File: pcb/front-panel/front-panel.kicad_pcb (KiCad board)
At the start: 2 copper layers, 85.7 x 19 mm, 31 parts, among them J1 HEADER-1x06, J2 HEADER-1x01, J3 HEADER-1x01, J4 HEADER-1x01, J5 HEADER-1x01, U1 ER-OLED1602-4W, U2 LT1109CS8-12

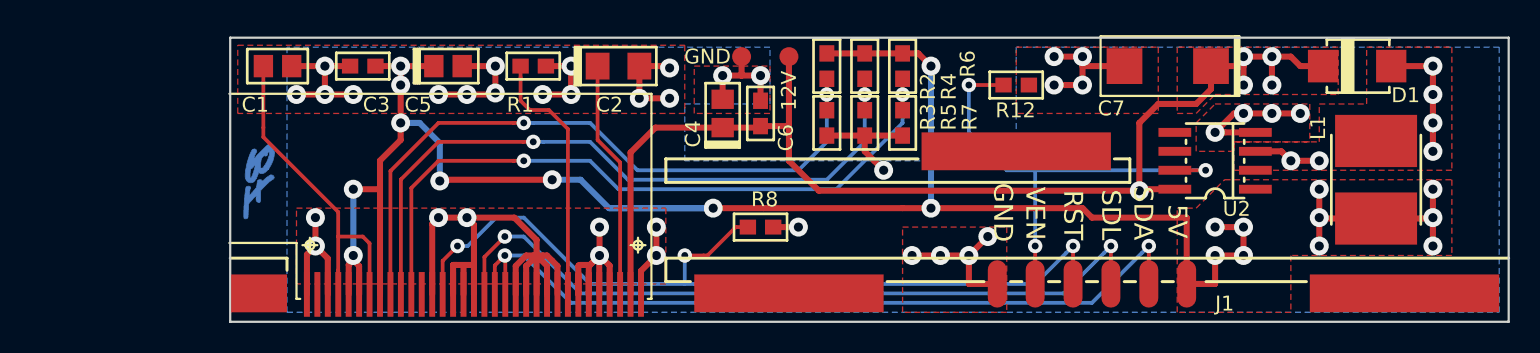
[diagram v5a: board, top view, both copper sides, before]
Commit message: Revised touch and front panel PCB, Added Motherboard PCB
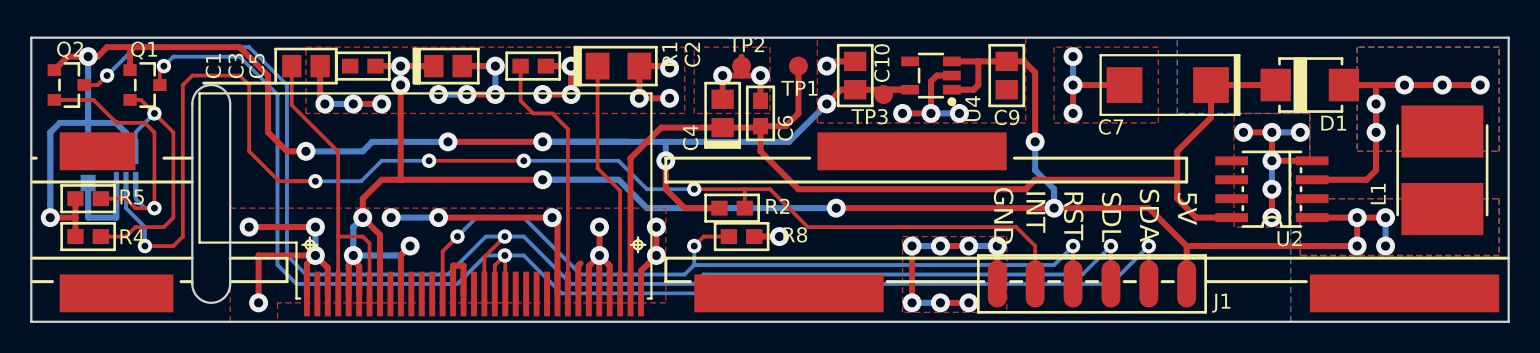
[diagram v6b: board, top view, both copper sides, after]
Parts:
- removed R12: 10k, SMT:R-0603
- removed R3, R7: 0, SMT:R-0603
- removed R6: DNP, SMT:R-0603
- removed the REF** at (96.5, 143.5)
- removed the REF** at (104.8, 134.0)
- removed the REF** at (179.3, 127.6)
- removed the REF** at (102.9, 149.9)
- added C10: 3.3uF, smt:C-0805, F.Cu at (144.8, 127.0)
- added C8: 100nF, smt:C-0603, B.Cu at (93.3, 133.3)
- added C9: 1uF, smt:C-0805, F.Cu at (154.9, 127.0)
- added J6: HEADER-1x01, conn-wire-pads:SolderPad-100x300, F.Cu at (94.0, 132.1)
- added Q1: BSS138, smt-sot:SOT23, F.Cu at (97.2, 127.6)
- added Q2: BSS138, smt-sot:SOT23, F.Cu at (92.1, 127.6)
- added REF**: VAL**, symbols:LOGO-OSHW-150, B.Cu at (184.4, 139.8)
- added REF**: VAL**, symbols:SIGNATURE_SILK, B.Cu at (175.0, 127.5)
- added TP3: 3.3V, conn-wire-pads:TEST-POINT-50, F.Cu at (146.7, 128.3)
- added U3: TSL2591, smt-dfn:DFN6, B.Cu at (95.9, 133.2)
- added U4: LP2981-33DBVT, smt-sot:SOT23-5, F.Cu at (149.9, 127.0)
- C1: footprint SMT:C-0805 -> smt:C-0805
- C2: footprint SMT:CPL-1206 -> smt:CPL-1206
- C3, C6: footprint SMT:C-0603 -> smt:C-0603
- C4: footprint SMT:CPL-0805 -> smt:CPL-0805
- C5: value 10uF -> 4.7uF; footprint SMT:CPL-0805 -> smt:CPL-0805
- C7: footprint SMT:CPL-2312 -> smt:CPL-2312
- D1: footprint SMT:DO-214-AA -> smt:DO-214-AA
- J1: footprint Conn-Wire-Pads:WP-50mil-1x06 -> conn-wire-pads:WP-50mil-1x06
- J2, J3, J4: footprint Conn-Wire-Pads:SolderPad-100x500 -> conn-wire-pads:SolderPad-100x500
- J5: footprint Conn-Wire-Pads:SolderPad-100x150 -> conn-wire-pads:SolderPad-100x300
- L1: footprint SMT:IND-CD54 -> smt:IND-CD54
- R1: value 470k -> 500k; footprint SMT:R-0603 -> smt:R-0603
- R2: value DNP -> 10k; footprint SMT:R-0603 -> smt:R-0603
- R4: value 0 -> 4.7k; footprint SMT:R-0603 -> smt:R-0603
- R5: value DNP -> 4.7k; footprint SMT:R-0603 -> smt:R-0603
- R8: footprint SMT:R-0603 -> smt:R-0603
- TP1, TP2: footprint Conn-Wire-Pads:TEST-POINT-50 -> conn-wire-pads:TEST-POINT-50
- U1: footprint Misc:LCD-ER-OLED1602 -> misc:LCD-ER-OLED1602
- U2: footprint SMT-SOIC:SOIC8 -> smt-soic:SOIC8
- moved R4 53.3 mm to (93.3, 137.8), turned to 180 degrees
- moved R5 52.3 mm to (93.3, 135.3), turned to 180 degrees
- moved R2 11.4 mm to (136.5, 135.9), turned to 180 degrees
- moved J5 9.53 mm to (95.2, 141.6)
- moved J4 6.98 mm to (148.6, 132.1)
- moved L1 4.49 mm to (184.2, 133.3)
- moved U2 4.26 mm to (172.7, 134.6)
- moved D1 3.42 mm to (175.3, 127.6)
- moved C1 1.91 mm to (108.0, 126.4)
- moved R8 1.42 mm to (137.2, 137.8)
- moved C7 1.27 mm to (165.7, 127.6)
- moved TP1 0.90 mm to (141.0, 126.4)
- moved TP2 0.63 mm to (137.2, 126.4)
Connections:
- J1 pad 5: /VCC_EN -> /INT
- R2 pad 1: +5V -> /INT
- R2 pad 2: Net-(R2-Pad2) -> +3V3
- R4 pad 1: +5V -> /SDA_3V3
- R4 pad 2: Net-(R4-Pad2) -> +3V3
- R5 pad 1: Net-(R4-Pad2) -> /SCL_3V3
- R5 pad 2: GND -> +3V3
- U1 pad 10: Net-(R4-Pad2) -> +5V
- U1 pad 11: Net-(R6-Pad2) -> GND
- U1 pad 9: Net-(R2-Pad2) -> GND
- U2 pad 7: /VCC_EN -> Net-(U2-Pad7)
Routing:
- net +3V3: track 0.00 -> 104.9 mm, vias 0 -> 7
- net /INT: track 0.00 -> 88.4 mm, vias 0 -> 5
- net Net-(R6-Pad2): track 47.5 -> 0.00 mm, vias 2 -> 0
- net Net-(R4-Pad2): track 47.2 -> 0.00 mm, vias 2 -> 0
- net Net-(R2-Pad2): track 46.3 -> 0.00 mm, vias 2 -> 0
- net /SCL: track 50.5 -> 93.3 mm, vias 2 -> 3
- net /SDA: track 54.1 -> 91.9 mm, vias 2 -> 3
- net /VCC_EN: track 32.1 -> 0.00 mm, vias 3 -> 0
- net /SCL_3V3: track 0.00 -> 19.0 mm, vias 0 -> 1
- net /SDA_3V3: track 0.00 -> 18.0 mm, vias 0 -> 1
- net /SW_12V: track 13.1 -> 21.3 mm, vias 6 -> 5
- net +5V: track 141.2 -> 135.1 mm, vias 20 -> 13
- net +12V: track 78.0 -> 72.8 mm, vias 5 -> 0
- net /~RESET: track 58.1 -> 54.9 mm
- net GND: track 144.2 -> 143.3 mm, vias 38 -> 47
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- added copper zone on B.Cu, net +5V
- added copper zone on B.Cu, net /SW_12V
- removed copper zone on F.Cu, net +12V
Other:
- board size 85.7 x 19 mm -> 99.1 x 19 mm
- rule trace_min: 0.2 -> 0.2032
- board text added: "INT"
- board text added: "REV. B"
- board text removed: "REV. A"
- board text removed: "VEN"

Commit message: Updated PCB design
+ Completed daughterboard PCB layout.
* Corrected soldermask clerance on front panel pcb.
- Removed input resistor on DIN for RGB lamp board.
* Modified PCB layout for PSU board.
* Updated gerber files.
* Updated schematics pdf, BOM.
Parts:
- removed J6: HEADER-1x01, conn-wire-pads:SolderPad-100x300
- added H5: HEADER-1x01, conn-wire-pads:SolderPad-100x200, F.Cu at (94.0, 132.1)
- renumbered J2 to H1, J3 to H2, J4 to H3, J5 to H4, R8 to R3
